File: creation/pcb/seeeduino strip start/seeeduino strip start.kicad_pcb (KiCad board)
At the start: 2 copper layers, 41 x 16 mm, 15 parts, among them J1 Conn_01x01_Pin, J10 Conn_01x01_Pin, J2 Conn_01x01_Pin, J3 Conn_01x01_Pin, J4 Conn_01x01_Pin, J5 Conn_01x01_Pin, J6 Conn_01x01_Pin, J7 Conn_01x01_Pin, J8 Conn_01x01_Pin, J9 Conn_01x01_Pin

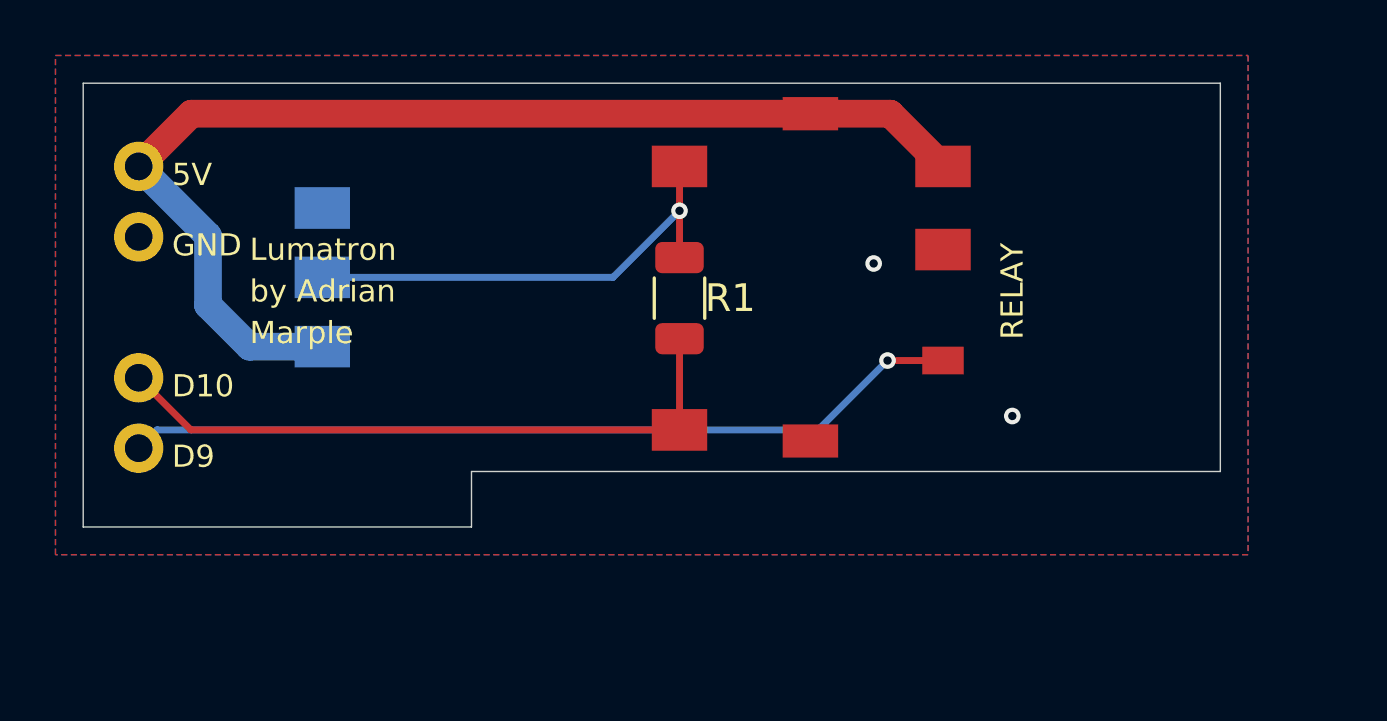
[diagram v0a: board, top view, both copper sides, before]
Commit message: Finalized new seeeduino strip start pcb design.
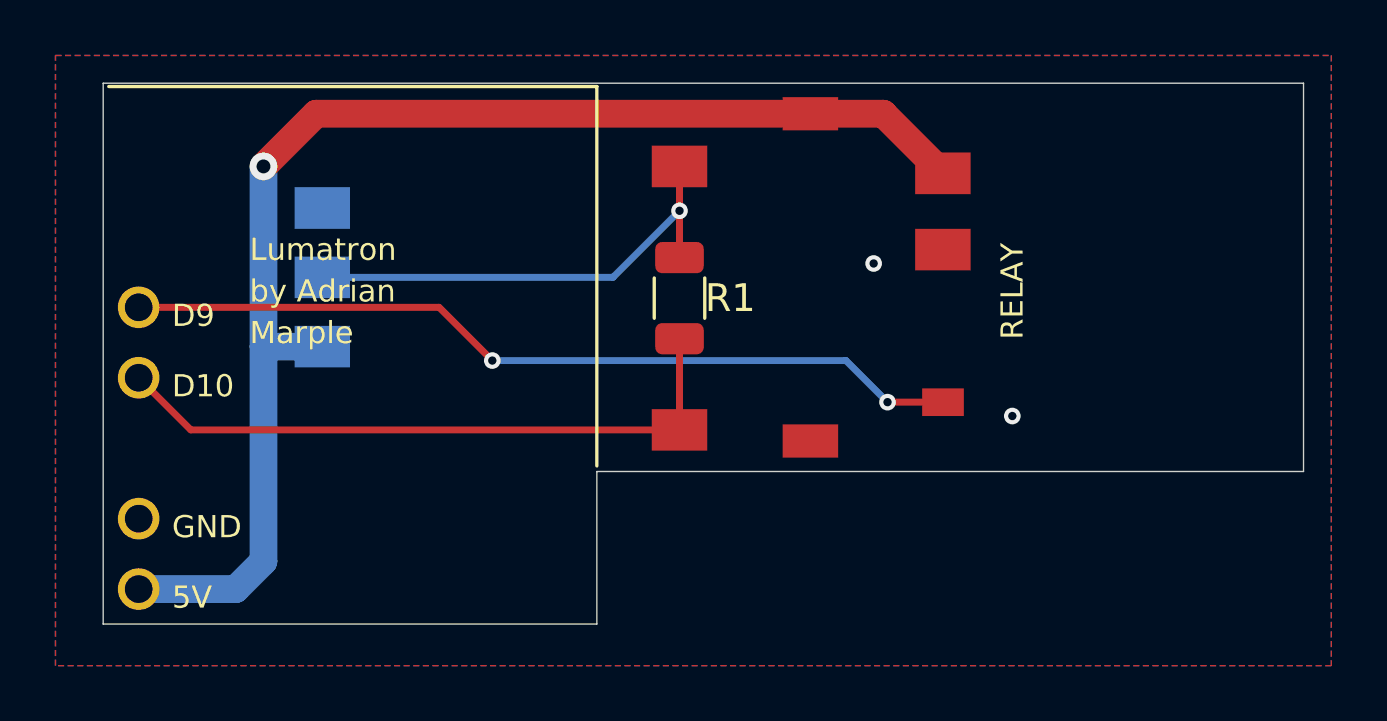
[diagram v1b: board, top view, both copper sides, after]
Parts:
- moved H1 15.2 mm to (102.0, 118.2)
- moved H2 10.2 mm to (102.0, 115.7)
- moved H4 5.08 mm to (102.0, 108.1)
- moved J8 1.50 mm to (131.0, 111.5)
- moved J6 0.25 mm to (131.0, 103.2)
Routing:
- net 5V: track 41.4 -> 47.5 mm, vias 0 -> 1
- net RLY: track 30.3 -> 30.4 mm, vias 1 -> 2
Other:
- board size 41 x 16 mm -> 43.3 x 19.5 mm
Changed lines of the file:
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@@
 	(footprint ""
 		(layer "F.Cu")
-		(at 131 110)
+		(at 131 111.5)
 		(descr "Wire Pad, Square, SMD Pad")
 		(property "Reference" "J8"
@@
 	(footprint ""
 		(layer "F.Cu")
-		(at 102 113.16)
+		(at 102 108.08)
 		(descr "Wire hole for a lead from the XIAO")
 		(property "Reference" "H4"
@@
 		(pad "1" thru_hole circle
 			(at 0 0)
-			(size 1.778 1.778)
+			(size 1.5 1.5)
 			(drill 1)
 			(layers "*.Cu" "*.Mask")
@@
 	(footprint ""
 		(layer "F.Cu")
-		(at 102 103)
+		(at 102 118.24)
 		(descr "Wire hole for a lead from the XIAO")
 		(property "Reference" "H1"
@@
 		(pad "1" thru_hole circle
 			(at 0 0)
-			(size 1.778 1.778)
+			(size 1.5 1.5)
 			(drill 1)
 			(layers "*.Cu" "*.Mask")
@@
 	(footprint ""
 		(layer "F.Cu")
-		(at 102 105.54)
+		(at 102 115.7)
 		(descr "Wire hole for a lead from the XIAO")
 		(property "Reference" "H2"
@@
 		(pad "1" thru_hole circle
 			(at 0 0)
-			(size 1.778 1.778)
+			(size 1.5 1.5)
 			(drill 1)
 			(layers "*.Cu" "*.Mask")
@@
 	(footprint ""
 		(layer "F.Cu")
-		(at 131 103)
+		(at 131 103.25)
 		(descr "Wire Pad, Square, SMD Pad")
 		(property "Reference" "J6"
@@
 		(pad "1" thru_hole circle
 			(at 0 0)
-			(size 1.778 1.778)
+			(size 1.5 1.5)
 			(drill 1)
 			(layers "*.Cu" "*.Mask")
@@
 	)
 	(gr_line
-		(start 114 116)
-		(end 100 116)
+		(start 118.52 100.12)
+		(end 118.52 113.8)
+		(stroke
+			(width 0.12)
+			(type default)
+		)
+		(layer "F.SilkS")
+	)
+	(gr_line
+		(start 100.92 100.12)
+		(end 118.52 100.12)
+		(stroke
+			(width 0.12)
+			(type default)
+		)
+		(layer "F.SilkS")
+	)
+	(gr_line
+		(start 118.52 119.5)
+		(end 100.72 119.5)
 		(stroke
 			(width 0.05)
@@
 	)
 	(gr_line
-		(start 100 100)
-		(end 141 100)
+		(start 100.72 100)
+		(end 144 100)
 		(stroke
 			(width 0.05)
@@
 	)
 	(gr_line
-		(start 141 100)
-		(end 141 114)
+		(start 144 100)
+		(end 144 114)
 		(stroke
 			(width 0.05)
@@
 	)
 	(gr_line
-		(start 141 114)
-		(end 114 114)
+		(start 144 114)
+		(end 118.52 114)
 		(stroke
 			(width 0.05)
@@
 	)
 	(gr_line
-		(start 100 116)
-		(end 100 100)
+		(start 100.72 119.5)
+		(end 100.72 100)
 		(stroke
 			(width 0.05)
@@
 	)
 	(gr_line
-		(start 114 114)
-		(end 114 116)
+		(start 118.52 114)
+		(end 118.52 119.5)
 		(stroke
 			(width 0.05)
@@
 	)
 	(gr_text "5V"
-		(at 103.2 103.3 0)
+		(at 103.2 118.54 0)
 		(layer "F.SilkS")
 		(effects
@@
 	)
 	(gr_text "D9"
-		(at 103.2 113.46 0)
+		(at 103.2 108.38 0)
 		(layer "F.SilkS")
 		(effects
@@
 	)
 	(gr_text "GND"
-		(at 103.2 105.84 0)
+		(at 103.2 116 0)
 		(layer "F.SilkS")
 		(effects
@@
 	)
 	(segment
-		(start 129.1 101.1)
-		(end 131 103)
+		(start 108.4 101.1)
+		(end 128.85 101.1)
 		(width 1)
 		(layer "F.Cu")
@@
 	)
 	(segment
-		(start 102 103)
-		(end 103.9 101.1)
+		(start 106.5 103)
+		(end 108.4 101.1)
 		(width 1)
 		(layer "F.Cu")
@@
 	)
 	(segment
-		(start 103.9 101.1)
-		(end 129.1 101.1)
+		(start 128.85 101.1)
+		(end 131 103.25)
 		(width 1)
 		(layer "F.Cu")
 		(net 2)
 	)
-	(segment
-		(start 104.5 105.5)
-		(end 104.5 108)
+	(via
+		(at 106.5 103)
+		(size 1)
+		(drill 0.5)
+		(layers "F.Cu" "B.Cu")
+		(net 2)
+	)
+	(segment
+		(start 106.5 117.24)
+		(end 106.5 103)
 		(width 1)
 		(layer "B.Cu")
@@
 	)
 	(segment
-		(start 106 109.5)
+		(start 105.5 118.24)
+		(end 106.5 117.24)
+		(width 1)
+		(layer "B.Cu")
+		(net 2)
+	)
+	(segment
+		(start 106.5 109.5)
 		(end 108.62 109.5)
 		(width 1)
@@
 	)
 	(segment
-		(start 104.5 108)
-		(end 106 109.5)
+		(start 102 118.24)
+		(end 105.5 118.24)
 		(width 1)
 		(layer "B.Cu")
@@
 	)
 	(segment
-		(start 102 103)
-		(end 104.5 105.5)
-		(width 1)
-		(layer "B.Cu")
-		(net 2)
-	)
-	(segment
 		(start 121.5 112.5)
 		(end 121.5 109.213)
@@
 	)
 	(segment
+		(start 102 110.62)
+		(end 103.88 112.5)
+		(width 0.25)
+		(layer "F.Cu")
+		(net 3)
+	)
+	(segment
 		(start 103.88 112.5)
 		(end 121.5 112.5)
-		(width 0.25)
-		(layer "F.Cu")
-		(net 3)
-	)
-	(segment
-		(start 102 110.62)
-		(end 103.88 112.5)
 		(width 0.25)
 		(layer "F.Cu")
@@
 	)
 	(segment
-		(start 129 110)
-		(end 131 110)
+		(start 112.83 108.08)
+		(end 114.75 110)
 		(width 0.25)
 		(layer "F.Cu")
 		(net 5)
 	)
+	(segment
+		(start 102 108.08)
+		(end 112.83 108.08)
+		(width 0.25)
+		(layer "F.Cu")
+		(net 5)
+	)
+	(segment
+		(start 129 111.5)
+		(end 131 111.5)
+		(width 0.25)
+		(layer "F.Cu")
+		(net 5)
+	)
 	(via
-		(at 129 110)
+		(at 114.75 110)
 		(size 0.6)
 		(drill 0.3)
@@
 		(net 5)
 	)
-	(segment
-		(start 126.5 112.5)
-		(end 129 110)
+	(via
+		(at 129 111.5)
+		(size 0.6)
+		(drill 0.3)
+		(layers "F.Cu" "B.Cu")
+		(net 5)
+	)
+	(segment
+		(start 114.75 110)
+		(end 127.5 110)
 		(width 0.25)
 		(layer "B.Cu")
@@
 	)
 	(segment
-		(start 102 113.16)
-		(end 102.66 112.5)
-		(width 0.25)
-		(layer "B.Cu")
-		(net 5)
-	)
-	(segment
-		(start 102.66 112.5)
-		(end 126.5 112.5)
+		(start 127.5 110)
+		(end 129 111.5)
 		(width 0.25)
 		(layer "B.Cu")
@@
 		(polygon
 			(pts
-				(xy 99 99) (xy 142 99) (xy 142 117) (xy 99 117)
-			)
-		)
+				(xy 99 99) (xy 145 99) (xy 145 121) (xy 99 121)
+			)
+		)
